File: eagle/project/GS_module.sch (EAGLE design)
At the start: 28 parts, among them Q2 MOSFET-PCHANNELFQP27P06, U1 V_REG_317SMD

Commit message: finish version 1.0 of GS board
yay!
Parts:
- removed C18, C4, C5: 0.1uF, rcl:C-EUC1206
- removed C19: 1uF, rcl:C-EUC1206
- removed C26: 0.1uF, resistor:C-EUC1206
- removed CANCONN: (no value), con-wago-508:W237-02P
- removed D1: 1N4004, diode:1N4004
- removed D3: 7.5V, diode:ZENER-DIODEZD-7.5
- removed LED1: FUSE HERE, LilyPad-Wearables:LED1206
- removed R25: 240, rcl:R-EU_R1206
- removed R26: 680, rcl:R-EU_R1206
- removed R27: 33, rcl:R-EU_R1206
- removed S2: DIRTY 5V, SparkFun-Electromechanical:SWITCH-SPDTKIT
- removed U$8: DISP_CONN, custom:DISP_CONN
- removed U1: V_REG_317SMD, SparkFun-PowerIC:V_REG_317SMD
- added CLUTCH_SW: (no value), con-wago-508:W237-02P
- added ENDSTOPS, MOTECSIGNAL, SHIFT: (no value), con-wago-508:W237-03P
- added MODE_SEL: (no value), con-wago-508:W237-05P
- added R1, R2: 27, rcl:R-EU_R1206
- added R10, R11, R12, R13, R14, R15, R16, R17, R18: 10k, rcl:R-EU_R1206
- added R3, R4: 15, rcl:R-EU_R1206
- added R6: 270, resistor:R-EU_R1206
- added R7: 10k, resistor:R-EU_R1206
- added R8: 4.7k, resistor:R-EU_R1206
- added R9: 1k, resistor:R-EU_R1206
- added U$17: OPTOISOLATOR-2SOIC8, SparkFun-DiscreteSemi:OPTOISOLATOR-2SOIC8
- added U$3: NPN_TRAN, custom:NPN_TRAN
- added U$4: PNP_TRAN, custom:PNP_TRAN
- renumbered JP4 to SOLDVR1, JP5 to SOLDVR2
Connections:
- removed net +5V/1: S2.S
- removed net +5VCLEAN: C4.2, S1.S, U$5.+VO, U$8.VCC
- removed net N$15: C26.1, D3.C, LED1.C, S2.P
- removed net N$17: C19.1, D1.A, LED1.A, R25.2, U1.OUT
- removed net N$37: R26.1, R27.2
- removed net N$38: R25.1, R26.2, U1.ADJ
- new net +5V: S1.S, SOLDVR1.10, SOLDVR2.10, U$17.CL1, U$5.+VO
- new net +5V/4: MOTECSIGNAL-1.KL, R7.1, U$4.E
- new net GND4: MOTECSIGNAL-3.KL, U$17.C1, U$3.E
- new net N$1: R7.2, U$3.C, U$4.B
- new net N$10: SOLDVR1.1, SOLDVR2.1
- new net N$3: R3.2, SOLDVR1.2
- new net N$4: R6.1, U$17.A1
- new net N$5: R4.2, SOLDVR2.2
- new net N$6: R6.2, U$4.C
- new net N$8: R8.1, U$3.B
- new net N$9: MOTECSIGNAL-2.KL, R8.2
- net +12V: no longer C18.1, D1.C, U1.IN
- net +3V3: now also R10.2, R11.2, R12.2, R13.2, R14.2, R15.2, R16.2, R17.2, R18.2; no longer C5.2, U$8.VI2C
- net AGND: now also R1.1, R2.1
- net GND: now also CLUTCH_SW-1.KL, ENDSTOPS-1.KL, MODE_SEL-5.KL, R9.2, SHIFT-1.KL, SOLDVR1.9, SOLDVR2.9; no longer C4.1, C5.1, U$8.GND
- net GNDI: no longer C18.2, C19.2, C26.2, D3.A, R27.1, S2.O
- net P10: now also SOLDVR2.6
- net P13: now also R9.1, U$17.EM1
- net P14: now also R10.1, SHIFT-3.KL
- net P15: now also R11.1, SHIFT-2.KL
- net P16: now also R1.2, R3.1
- net P17: now also ENDSTOPS-3.KL, R12.1
- net P18: now also ENDSTOPS-2.KL, R13.1; no longer U$8.I2CDAT
- net P19: now also R2.2, R4.1; no longer U$8.I2CCLK
- net P2: now also SOLDVR1.5
- net P20: now also MODE_SEL-4.KL, R14.1
- net P21: now also MODE_SEL-3.KL, R15.1
- net P22: now also MODE_SEL-2.KL, R16.1
- net P23: now also MODE_SEL-1.KL, R17.1
- net P3: now also SOLDVR1.8; no longer CANCONN-1.KL
- net P4: now also SOLDVR1.7; no longer CANCONN-2.KL
- net P5: now also SOLDVR1.6
- net P6: now also CLUTCH_SW-2.KL, R18.1
- net P7: now also SOLDVR2.5
- net P8: now also SOLDVR2.8
- net P9: now also SOLDVR2.7
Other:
- note added: "TO DIRTY"

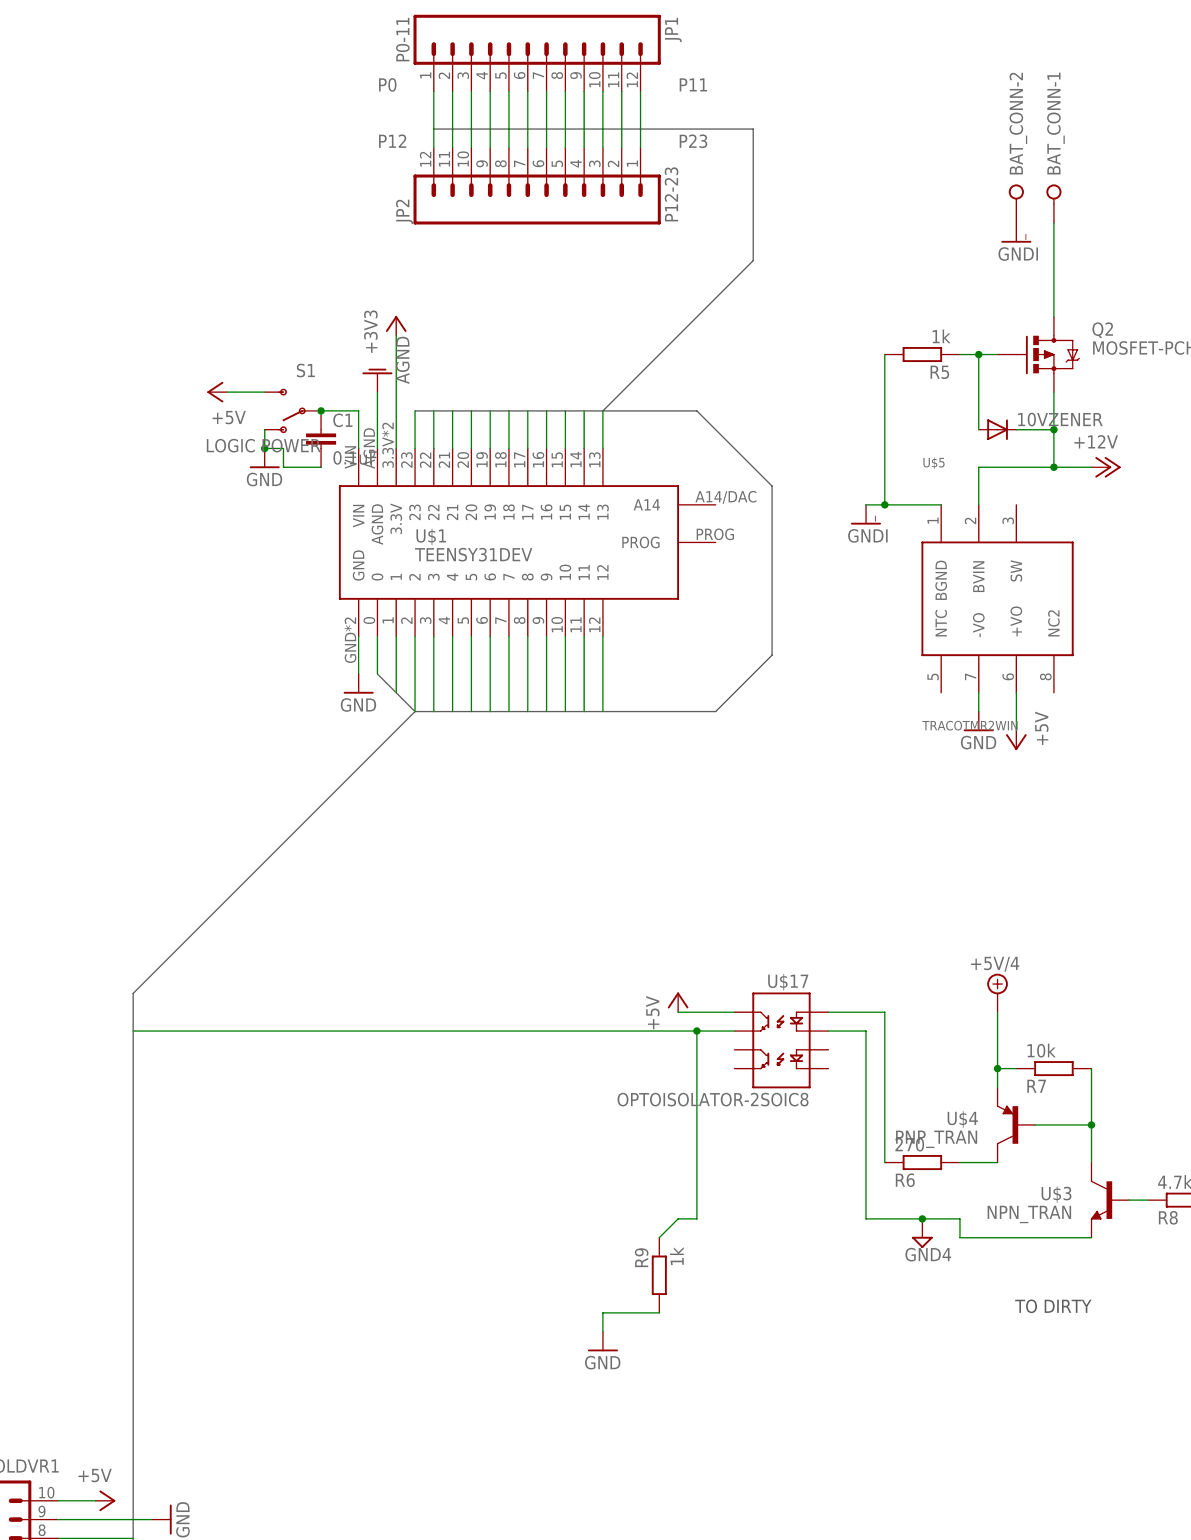
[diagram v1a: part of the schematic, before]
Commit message: Versions of the board which went to the fab house
Updating BOMS for component ordering
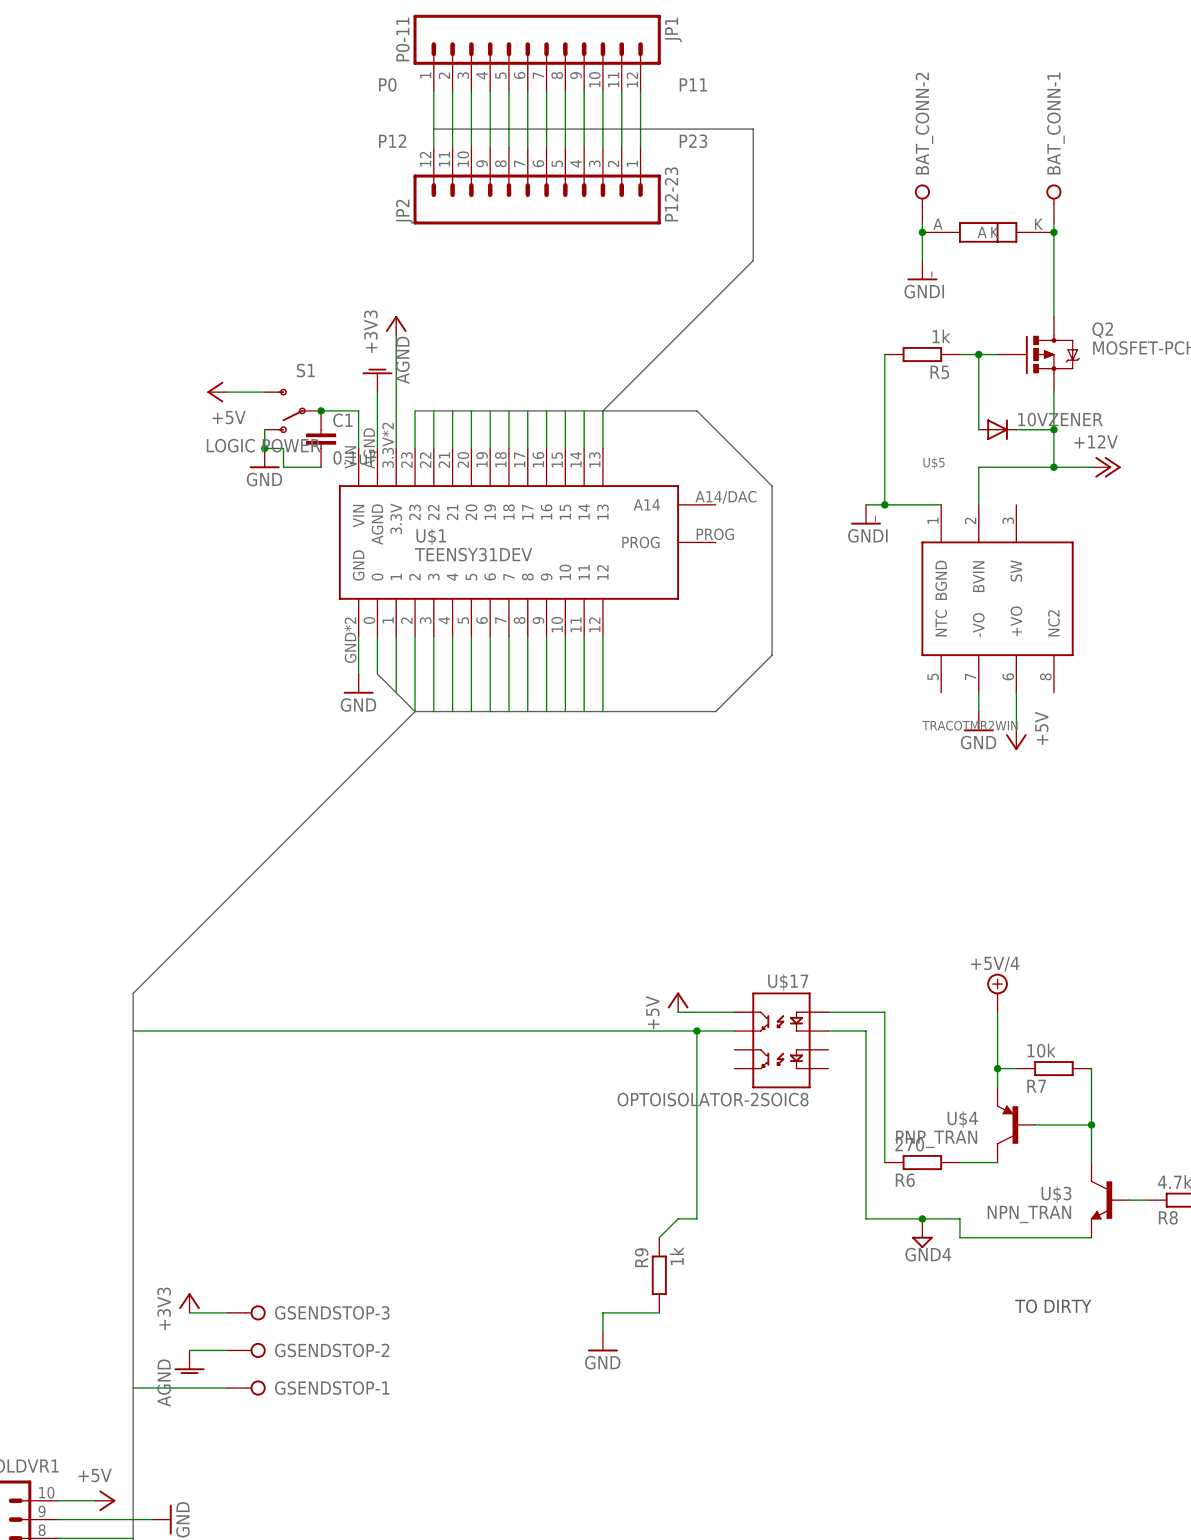
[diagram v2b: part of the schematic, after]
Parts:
- added GSENDSTOP: (no value), con-wago-508:W237-03P
- added U$6: LNBTVS, custom:LNBTVS
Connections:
- net +3V3: now also GSENDSTOP-3.KL
- net AGND: now also GSENDSTOP-2.KL
- net GNDI: now also U$6.A
- net N$13: now also U$6.K
- net P11: now also R10.1, SHIFT-3.KL
- net P12: now also R11.1, SHIFT-2.KL
- net P14: now also GSENDSTOP-1.KL; no longer R10.1, SHIFT-3.KL
- net P15: no longer R11.1, SHIFT-2.KL
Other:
- moved on the sheet: BAT_CONN-2
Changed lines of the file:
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@@
 <part name="GND15" library="supply1" deviceset="GND" device=""/>
 <part name="GND16" library="supply1" deviceset="GND" device=""/>
+<part name="GSENDSTOP" library="con-wago-508" deviceset="W237-03P" device=""/>
+<part name="AGND4" library="supply1" deviceset="AGND" device=""/>
+<part name="+3V11" library="supply1" deviceset="+3V3" device=""/>
+<part name="U$6" library="custom" deviceset="LNBTVS" device=""/>
 </parts>
 <sheets>
@@
 <instance part="R5" gate="G$1" x="55.88" y="25.4" rot="R180"/>
 <instance part="BAT_CONN" gate="-1" x="73.66" y="48.26" rot="R270"/>
-<instance part="BAT_CONN" gate="-2" x="68.58" y="48.26" rot="R270"/>
-<instance part="GNDI4" gate="G$1" x="68.58" y="40.64"/>
+<instance part="BAT_CONN" gate="-2" x="55.88" y="48.26" rot="R270"/>
+<instance part="GNDI4" gate="G$1" x="55.88" y="35.56"/>
 <instance part="AGND1" gate="VR1" x="-17.78" y="22.86" rot="R180"/>
 <instance part="JP3" gate="G$1" x="-68.58" y="-200.66"/>
@@
 <instance part="GND15" gate="1" x="-45.72" y="-132.08" rot="R90"/>
 <instance part="GND16" gate="1" x="-45.72" y="-165.1" rot="R90"/>
+<instance part="GSENDSTOP" gate="-1" x="-33.02" y="-114.3" rot="R180"/>
+<instance part="GSENDSTOP" gate="-2" x="-33.02" y="-109.22" rot="R180"/>
+<instance part="GSENDSTOP" gate="-3" x="-33.02" y="-104.14" rot="R180"/>
+<instance part="AGND4" gate="VR1" x="-43.18" y="-111.76"/>
+<instance part="+3V11" gate="G$1" x="-43.18" y="-101.6"/>
+<instance part="U$6" gate="G$1" x="68.58" y="40.64"/>
 </instances>
 <busses>
@@
 <pinref part="BAT_CONN" gate="-2" pin="KL"/>
 <pinref part="GNDI4" gate="G$1" pin="GNDI"/>
+<wire x1="55.88" y1="38.1" x2="55.88" y2="41.91" width="0.1524" layer="91"/>
+<pinref part="U$6" gate="G$1" pin="A"/>
+<wire x1="55.88" y1="41.91" x2="55.88" y2="43.18" width="0.1524" layer="91"/>
+<junction x="55.88" y="41.91"/>
 </segment>
 </net>
@@
 <pinref part="R18" gate="G$1" pin="2"/>
 <pinref part="+3V10" gate="G$1" pin="+3V3"/>
+</segment>
+<segment>
+<pinref part="+3V11" gate="G$1" pin="+3V3"/>
+<pinref part="GSENDSTOP" gate="-3" pin="KL"/>
+<wire x1="-43.18" y1="-104.14" x2="-38.1" y2="-104.14" width="0.1524" layer="91"/>
 </segment>
 </net>
@@
 <wire x1="-2.54" y1="55.88" x2="-2.54" y2="53.34" width="0.1524" layer="91"/>
 </segment>
-<segment>
-<pinref part="R11" gate="G$1" pin="1"/>
-<wire x1="-30.48" y1="-259.08" x2="-10.16" y2="-259.08" width="0.1524" layer="91"/>
-<wire x1="-10.16" y1="-259.08" x2="-10.16" y2="-241.3" width="0.1524" layer="91"/>
-<pinref part="SHIFT" gate="-2" pin="KL"/>
-<wire x1="-10.16" y1="-241.3" x2="-5.08" y2="-241.3" width="0.1524" layer="91"/>
-<wire x1="-50.8" y1="-259.08" x2="-30.48" y2="-259.08" width="0.1524" layer="91"/>
-<junction x="-30.48" y="-259.08"/>
-</segment>
 </net>
 <net name="P14" class="0">
@@
 </segment>
 <segment>
-<pinref part="R10" gate="G$1" pin="1"/>
-<wire x1="-30.48" y1="-231.14" x2="-10.16" y2="-231.14" width="0.1524" layer="91"/>
-<wire x1="-10.16" y1="-231.14" x2="-10.16" y2="-236.22" width="0.1524" layer="91"/>
-<pinref part="SHIFT" gate="-3" pin="KL"/>
-<wire x1="-10.16" y1="-236.22" x2="-5.08" y2="-236.22" width="0.1524" layer="91"/>
-<wire x1="-50.8" y1="-231.14" x2="-30.48" y2="-231.14" width="0.1524" layer="91"/>
-<junction x="-30.48" y="-231.14"/>
+<pinref part="GSENDSTOP" gate="-1" pin="KL"/>
+<wire x1="-50.8" y1="-114.3" x2="-38.1" y2="-114.3" width="0.1524" layer="91"/>
 </segment>
 </net>
@@
 <label x="22.86" y="60.96" size="1.778" layer="91"/>
 </segment>
+<segment>
+<pinref part="R10" gate="G$1" pin="1"/>
+<wire x1="-30.48" y1="-231.14" x2="-10.16" y2="-231.14" width="0.1524" layer="91"/>
+<wire x1="-10.16" y1="-231.14" x2="-10.16" y2="-236.22" width="0.1524" layer="91"/>
+<pinref part="SHIFT" gate="-3" pin="KL"/>
+<wire x1="-10.16" y1="-236.22" x2="-5.08" y2="-236.22" width="0.1524" layer="91"/>
+<wire x1="-50.8" y1="-231.14" x2="-30.48" y2="-231.14" width="0.1524" layer="91"/>
+<junction x="-30.48" y="-231.14"/>
+</segment>
 </net>
 <net name="P12" class="0">
@@
 <wire x1="-10.16" y1="55.88" x2="-10.16" y2="53.34" width="0.1524" layer="91"/>
 <label x="-17.78" y="53.34" size="1.778" layer="91"/>
+</segment>
+<segment>
+<pinref part="R11" gate="G$1" pin="1"/>
+<wire x1="-30.48" y1="-259.08" x2="-10.16" y2="-259.08" width="0.1524" layer="91"/>
+<wire x1="-10.16" y1="-259.08" x2="-10.16" y2="-241.3" width="0.1524" layer="91"/>
+<pinref part="SHIFT" gate="-2" pin="KL"/>
+<wire x1="-10.16" y1="-241.3" x2="-5.08" y2="-241.3" width="0.1524" layer="91"/>
+<wire x1="-50.8" y1="-259.08" x2="-30.48" y2="-259.08" width="0.1524" layer="91"/>
+<junction x="-30.48" y="-259.08"/>
 </segment>
 </net>
@@
 <wire x1="73.66" y1="15.24" x2="68.58" y2="15.24" width="0.1524" layer="91"/>
 <wire x1="73.66" y1="15.24" x2="73.66" y2="10.16" width="0.1524" layer="91"/>
-<wire x1="73.66" y1="10.16" x2="63.5" y2="10.16" width="0.1524" layer="91"/>
-<pinref part="U$5" gate="G$1" pin="BVIN"/>
-<wire x1="63.5" y1="10.16" x2="63.5" y2="5.08" width="0.1524" layer="91"/>
 <wire x1="73.66" y1="10.16" x2="78.74" y2="10.16" width="0.1524" layer="91"/>
 <pinref part="P+2" gate="1" pin="+12V"/>
 <junction x="73.66" y="15.24"/>
+<wire x1="73.66" y1="10.16" x2="63.5" y2="10.16" width="0.1524" layer="91"/>
 <junction x="73.66" y="10.16"/>
+<pinref part="U$5" gate="G$1" pin="BVIN"/>
+<wire x1="63.5" y1="10.16" x2="63.5" y2="5.08" width="0.1524" layer="91"/>
 </segment>
 </net>
@@
 <pinref part="BAT_CONN" gate="-1" pin="KL"/>
 <pinref part="Q2" gate="G$1" pin="D"/>
-<wire x1="73.66" y1="43.18" x2="73.66" y2="30.48" width="0.1524" layer="91"/>
+<wire x1="73.66" y1="43.18" x2="73.66" y2="41.91" width="0.1524" layer="91"/>
+<pinref part="U$6" gate="G$1" pin="K"/>
+<wire x1="73.66" y1="41.91" x2="73.66" y2="30.48" width="0.1524" layer="91"/>
+<junction x="73.66" y="41.91"/>
 </segment>
 </net>
@@
 <pinref part="AGND3" gate="VR1" pin="AGND"/>
 </segment>
-</net>
+<segment>
+<pinref part="AGND4" gate="VR1" pin="AGND"/>
+<pinref part="GSENDSTOP" gate="-2" pin="KL"/>
+<wire x1="-43.18" y1="-109.22" x2="-38.1" y2="-109.22" width="0.1524" layer="91"/>
+</segment>
+</net>
